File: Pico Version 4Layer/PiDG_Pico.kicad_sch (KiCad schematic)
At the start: 45 parts, among them J1 Conn_02x05_Odd_Even, J10 Trig, J11 Laser Enable, J12 Pixel Reset, J14 Pico Socket A, J15 Pico Socket B, J16 Laser En/PWM Trig/GND, J2 Conn_02x05_Odd_Even, J3 Conn_02x05_Odd_Even, J4 Conn_02x05_Odd_Even, J5 Conn_02x05_Odd_Even, J6 Conn_02x05_Odd_Even, J7 Laser 1, J8 Laser 2, U1 74LVC1G04, U10 74LVC1G08, U11 Raspberry Pi Pico 2 W, U12 74LVC1G17, U13 UCC27524, U2 SN74LVC04AD, U3 74LVC1G04, U4 SN74LVC04AD, U5 74LVC1G04, U6 SN74LVC04AD, U7 74LVC1G08, U8 74LVC1G08, U9 NCP718xSN180

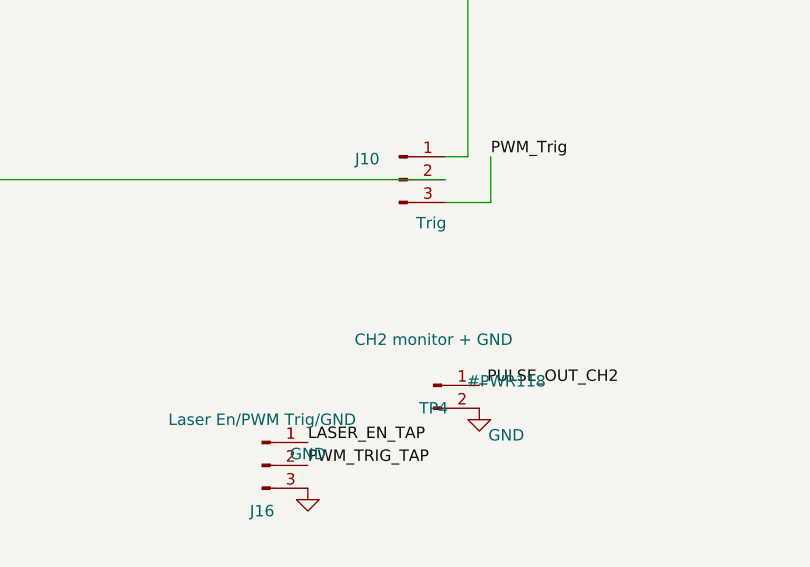
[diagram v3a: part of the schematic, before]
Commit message: Add R9 pull-down on the J10 camera-trigger select node
With no shunt fitted on J10, PWM_TRIG_TAP (J10.2, J16.2, U5.2) had no
defined level: U5's input floated on ~145 mm of trace, which also runs
up across the board to J16.2, and all six camera trigger lines followed
it.

R9 (10k, 0805) now pulls it to GND, so with J10 unshunted the triggers
idle low -- their inactive state. 10k rather than a weaker pull: U5 runs
from the 1.8 V rail (VIL 0.63 V), and at the datasheet's worst-case 5 uA
input leakage 100k would sit at 0.5 V with only 0.13 V to spare, where
10k holds it at 0.05 V and rejects coupled noise ten times better. The
selected GPIO sees an extra 330 uA when J10 is shunted. Same value as R8,
so no new BOM line.

Placed at (203.5, 106) rot 90 beside U5's input run with a 2 mm link;
worst-case clearance 1.09 mm. B.Cu copper runs directly underneath, so
its ground pad connects through the F.Cu pour rather than a via --
confirmed by the kicad-cli unconnected-items check.

Hardware.md: J10 open item removed; the laser-impedance item reworded to
make clear J7/J8 are outputs and the impedance in question is the
laser's own trigger input at the far end of the cable.

ERC 0, DRC 0, 0 unconnected items, board vs schematic nets exact.

Co-Authored-By: Claude Opus 5.5 (1M context) <noreply@anthropic.com>
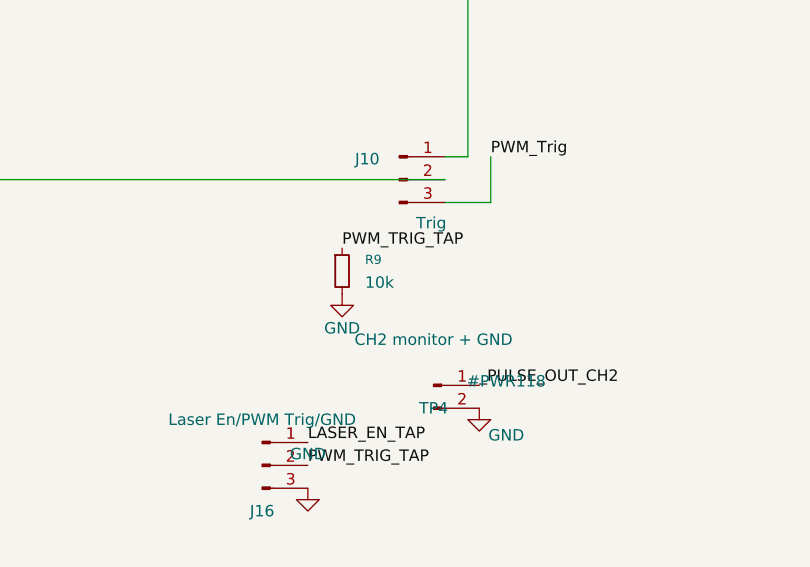
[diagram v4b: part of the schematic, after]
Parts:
- added R9: 10k, Resistor_SMD:R_0805_2012Metric_Pad1.20x1.40mm_HandSolder, symbol Device:R_Small
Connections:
- net GND: now also R9.2
- net PWM_TRIG_TAP: now also R9.1
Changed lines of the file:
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@@
 		)
 	)
+	(label "PWM_TRIG_TAP"
+		(at 279.4 175.26000000000002 0)
+		(effects
+			(font
+				(size 1.27 1.27)
+			)
+			(justify left bottom)
+		)
+	)
 	(label "LASER_EN_JMP"
 		(at 372.11 99.06 0)
@@
 					(unit 1)
 				)
+			)
+		)
+	)
+	(symbol
+		(lib_id "Device:R_Small")
+		(at 279.4 177.8 0)
+		(unit 1)
+		(body_style 1)
+		(exclude_from_sim no)
+		(in_bom yes)
+		(on_board yes)
+		(in_pos_files yes)
+		(dnp no)
+		(fields_autoplaced yes)
+		(property "Reference" "R9"
+			(at 281.94 176.5299 0)
+			(show_name no)
+			(do_not_autoplace no)
+			(effects
+				(font
+					(size 1.016 1.016)
+				)
+				(justify left)
+			)
+		)
+		(property "Value" "10k"
+			(at 281.94 179.06990000000002 0)
+			(show_name no)
+			(do_not_autoplace no)
+			(effects
+				(font
+					(size 1.27 1.27)
+				)
+				(justify left)
+			)
+		)
+		(property "Footprint" "Resistor_SMD:R_0805_2012Metric_Pad1.20x1.40mm_HandSolder"
+			(at 279.4 177.8 0)
+			(hide yes)
+			(show_name no)
+			(do_not_autoplace no)
+			(effects
+				(font
+					(size 1.27 1.27)
+				)
+			)
+		)
+		(property "Datasheet" ""
+			(at 279.4 177.8 0)
+			(hide yes)
+			(show_name no)
+			(do_not_autoplace no)
+			(effects
+				(font
+					(size 1.27 1.27)
+				)
+			)
+		)
+		(property "Description" "Pull-down on PWM_TRIG_TAP: defines U5 input when J10 has no shunt"
+			(at 279.4 177.8 0)
+			(hide yes)
+			(show_name no)
+			(do_not_autoplace no)
+			(effects
+				(font
+					(size 1.27 1.27)
+				)
+			)
+		)
+		(pin "2"
+		)
+		(pin "1"
+		)
+		(instances
+			(project "PiDG_Pico"
+				(path "/e63e39d7-6ac0-4ffd-8aa3-1841a4541b55"
+					(reference "R9")
+					(unit 1)
+				)
+			)
+		)
+	)
+	(symbol
+		(lib_id "power:GND")
+		(at 279.4 180.34 0)
+		(unit 1)
+		(body_style 1)
+		(exclude_from_sim no)
+		(in_bom yes)
+		(on_board yes)
+		(in_pos_files yes)
+		(dnp no)
+		(fields_autoplaced yes)
+		(property "Reference" "#PWR120"
+			(at 282.4 177.34 0)
+			(hide yes)
+			(show_name no)
+			(do_not_autoplace no)
+			(effects
+				(font
+					(size 1.27 1.27)
+				)
+			)
+		)
+		(property "Value" "GND"
+			(at 279.4 184.15 0)
+			(show_name no)
+			(do_not_autoplace no)
+			(effects
+				(font
+					(size 1.27 1.27)
+				)
+			)
+		)
+		(property "Footprint" ""
+			(at 279.4 180.34 0)
+			(hide yes)
+			(show_name no)
+			(do_not_autoplace no)
+			(effects
+				(font
+					(size 1.27 1.27)
+				)
+			)
+		)
+		(property "Datasheet" ""
+			(at 279.4 180.34 0)
+			(hide yes)
+			(show_name no)
+			(do_not_autoplace no)
+			(effects
+				(font
+					(size 1.27 1.27)
+				)
+			)
+		)
+		(property "Description" "Power symbol creates a global label with name \"GND\""
+			(at 279.4 180.34 0)
+			(hide yes)
+			(show_name no)
+			(do_not_autoplace no)
+			(effects
+				(font
+					(size 1.27 1.27)
+				)
+			)
+		)
+		(pin "1"
+		)
+		(instances
+			(project "PiDG_Pico"
+				(path "/e63e39d7-6ac0-4ffd-8aa3-1841a4541b55"
+					(reference "#PWR120")
+					(unit 1)
+				)

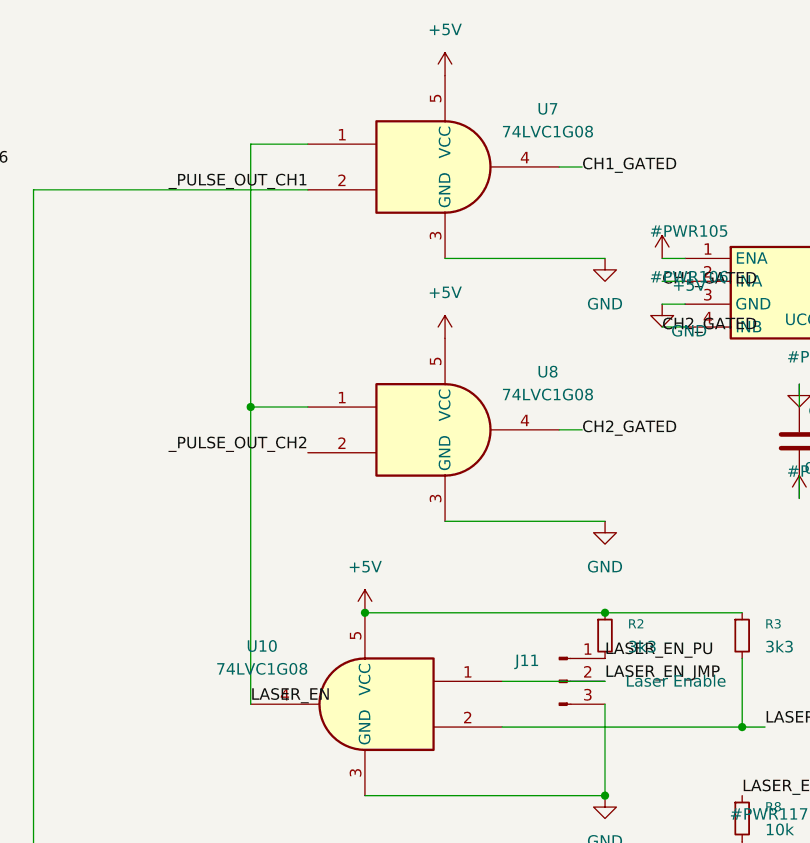
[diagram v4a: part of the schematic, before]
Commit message: Laser path: AHCT gates, firmware safety limits for PicoLas LDP-V drivers
The laser outputs must trigger PicoLas LDP-V 10-70 and LDP-V 240-100
drivers. This commit fixes the two problems in that path that need no
design decision. The third -- output amplitude -- is documented as the
blocking open item pending a choice of supply for a 10 V driver rail.

U7, U8, U10: 74LVC1G08 -> 74AHCT1G08
- At VCC = 5 V an LVC input needs 0.7 x VCC = 3.5 V to read high, but
  U7/U8 take their pulses straight from 3.3 V Pico GPIOs -- outside the
  guaranteed operating range at every normal USB voltage. AHCT has TTL
  input thresholds (high above 2.0 V): ~1.3 V of margin.
- U10 swapped too: the J11/R2/R8 arming divider now clears VIH by 1.76 V
  instead of ~260 mV, and an external interlock on J16.1 can be 3.3 V.
- 74AHCT1G08 extends 74LVC1G08 in the KiCad library: same body, same
  pins, same SOT-23-5 footprint. No wiring or layout change.

Firmware laser safety limits
- LDP-V 10-70: 10 ns - 1 us pulse, max duty factor 0.1 %.
  LDP-V 240-100: 60 ns - >1 us, 7.5 %. CH1/CH2 share one width, so the
  10-70 governs.
- The previous default -- 2 us at 1 kHz -- was twice the 10-70's maximum
  pulse width and twice its duty limit, applied at power-up before any
  command was sent.
- Default WIDTH is now 100 ns, inside both drivers' ranges.
- applyPulseParams() rejects WIDTH > 1000 ns or WIDTH x FREQ > 0.1 %
  (kLaserMaxWidthNs, kLaserMaxDutyPpm). HELP text states the limits.

Documented, not yet fixed: the LDP-V trigger inputs are 50 ohm
terminated and need 4.5-5.2 V high / <= 0.2 V low. Today's 5 V rail
through 47 ohm delivers 2.1-2.6 V; 0 ohm series still spans 3.8-5.0 V.
A regulated 10 V rail with R6/R7 = 48.7 ohm gives 4.55-5.11 V across all
tolerances.

ERC 0, DRC 0, 0 unconnected. Firmware builds.

Co-Authored-By: Claude Opus 5.5 (1M context) <noreply@anthropic.com>
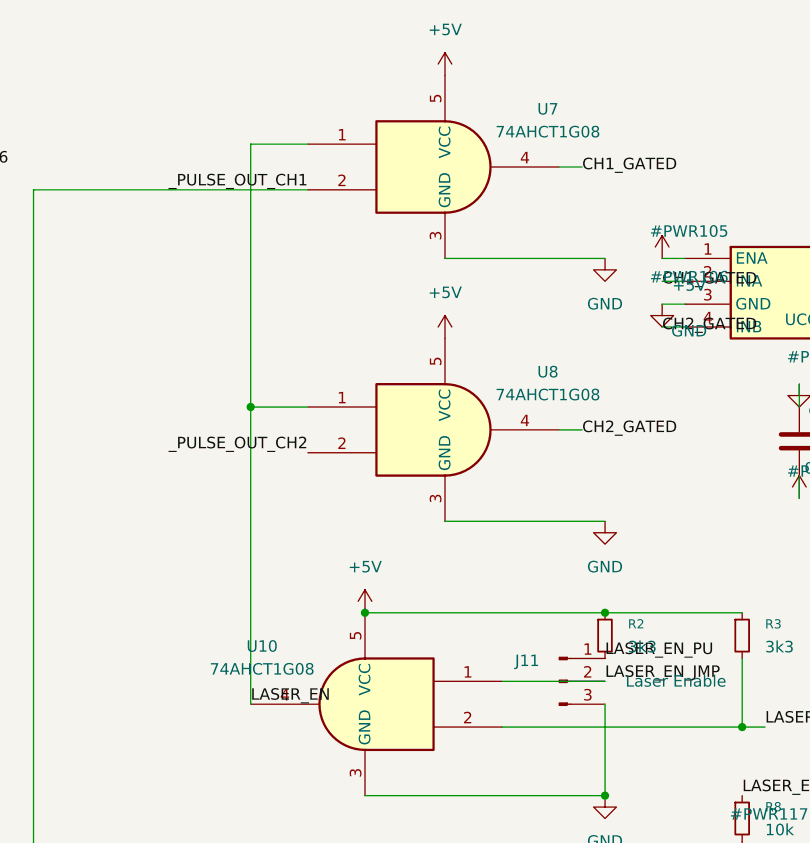
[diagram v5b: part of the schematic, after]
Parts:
- U10, U7, U8: value 74LVC1G08 -> 74AHCT1G08; symbol 74xGxx:74LVC1G08 -> 74xGxx:74AHCT1G08
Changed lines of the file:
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@@
 	)
 	(symbol
-		(lib_id "74xGxx:74LVC1G08")
+		(lib_id "74xGxx:74AHCT1G08")
 		(at 339.09 58.42 0)
 		(unit 1)
@@
 			)
 		)
-		(property "Value" "74LVC1G08"
+		(property "Value" "74AHCT1G08"
 			(at 350.52 54.5398 0)
 			(show_name no)
@@
 			)
 		)
-		(property "Datasheet" "https://www.ti.com/lit/ds/symlink/sn74lvc1g08.pdf"
+		(property "Datasheet" "http://www.ti.com/lit/sg/scyt129e/scyt129e.pdf"
 			(at 339.09 58.42 0)
 			(hide yes)
@@
 	)
 	(symbol
-		(lib_id "74xGxx:74LVC1G08")
+		(lib_id "74xGxx:74AHCT1G08")
 		(at 330.2 88.9 0)
 		(mirror y)
@@
 			)
 		)
-		(property "Value" "74LVC1G08"
+		(property "Value" "74AHCT1G08"
 			(at 318.77 85.0198 0)
 			(show_name no)
@@
 			)
 		)
-		(property "Datasheet" "https://www.ti.com/lit/ds/symlink/sn74lvc1g08.pdf"
+		(property "Datasheet" "http://www.ti.com/lit/sg/scyt129e/scyt129e.pdf"
 			(at 330.2 88.9 0)
 			(hide yes)
@@
 	)
 	(symbol
-		(lib_id "74xGxx:74LVC1G08")
+		(lib_id "74xGxx:74AHCT1G08")
 		(at 339.09 29.21 0)
 		(unit 1)
@@
 			)
 		)
-		(property "Value" "74LVC1G08"
+		(property "Value" "74AHCT1G08"
 			(at 350.52 25.3298 0)
 			(show_name no)
@@
 			)
 		)
-		(property "Datasheet" "https://www.ti.com/lit/ds/symlink/sn74lvc1g08.pdf"
+		(property "Datasheet" "http://www.ti.com/lit/sg/scyt129e/scyt129e.pdf"
 			(at 339.09 29.21 0)
 			(hide yes)
